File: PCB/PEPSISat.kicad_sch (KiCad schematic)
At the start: 2 parts, among them U1 STM32H747IITx, U2 RP2350A

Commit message: KiCad
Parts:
- added U3: MT48LC16M16A2P, Package_SO:TSOP-II-54_22.2x10.16mm_P0.8mm, symbol Memory_RAM:MT48LC16M16A2P
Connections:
- net at U1.110 (PG2): now also U3.36 (A12)
- net at U1.18 (PF0): now also U3.23 (A0)
- net at U1.19 (PF1): now also U3.24 (A1)
- net at U1.20 (PF2): now also U3.25 (A2)
- net at U1.21 (PF3): now also U3.26 (A3)
- net at U1.22 (PF4): now also U3.29 (A4)
- net at U1.23 (PF5): now also U3.30 (A5)
- net at U1.59 (PF12): now also U3.31 (A6)
- net at U1.60 (PF13): now also U3.32 (A7)
- net at U1.61 (PF14): now also U3.33 (A8)
- net at U1.62 (PF15): now also U3.34 (A9)
- net at U1.63 (PG0): now also U3.22 (A10)
- net at U1.66 (PG1): now also U3.35 (A11)
- new net: U3.1 (VDD), U3.14 (VDD), U3.27 (VDD)
- new net: U3.12 (VSSQ), U3.46 (VSSQ), U3.52 (VSSQ), U3.6 (VSSQ)
- new net: U3.28 (VSS), U3.41 (VSS), U3.54 (VSS)
- new net: U3.3 (VDDQ), U3.43 (VDDQ), U3.49 (VDDQ), U3.9 (VDDQ)
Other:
- moved on the sheet: U1

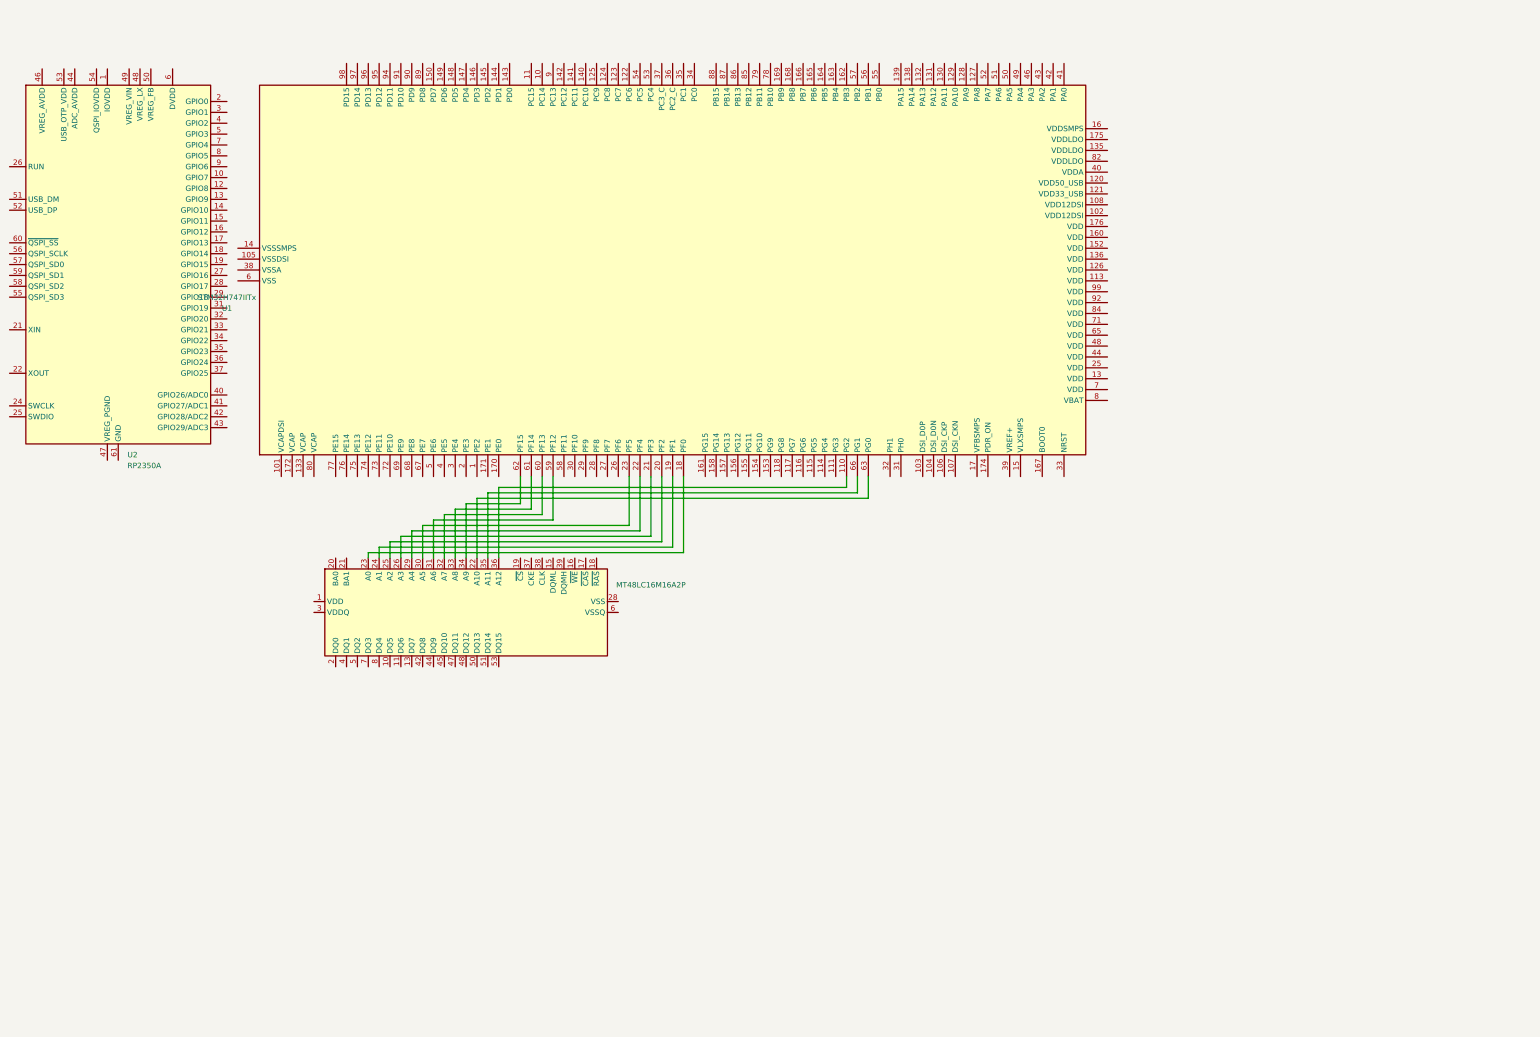
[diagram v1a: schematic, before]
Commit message: KiCad - RAM D&A bus
Added RAM connection for Data and Address bus.
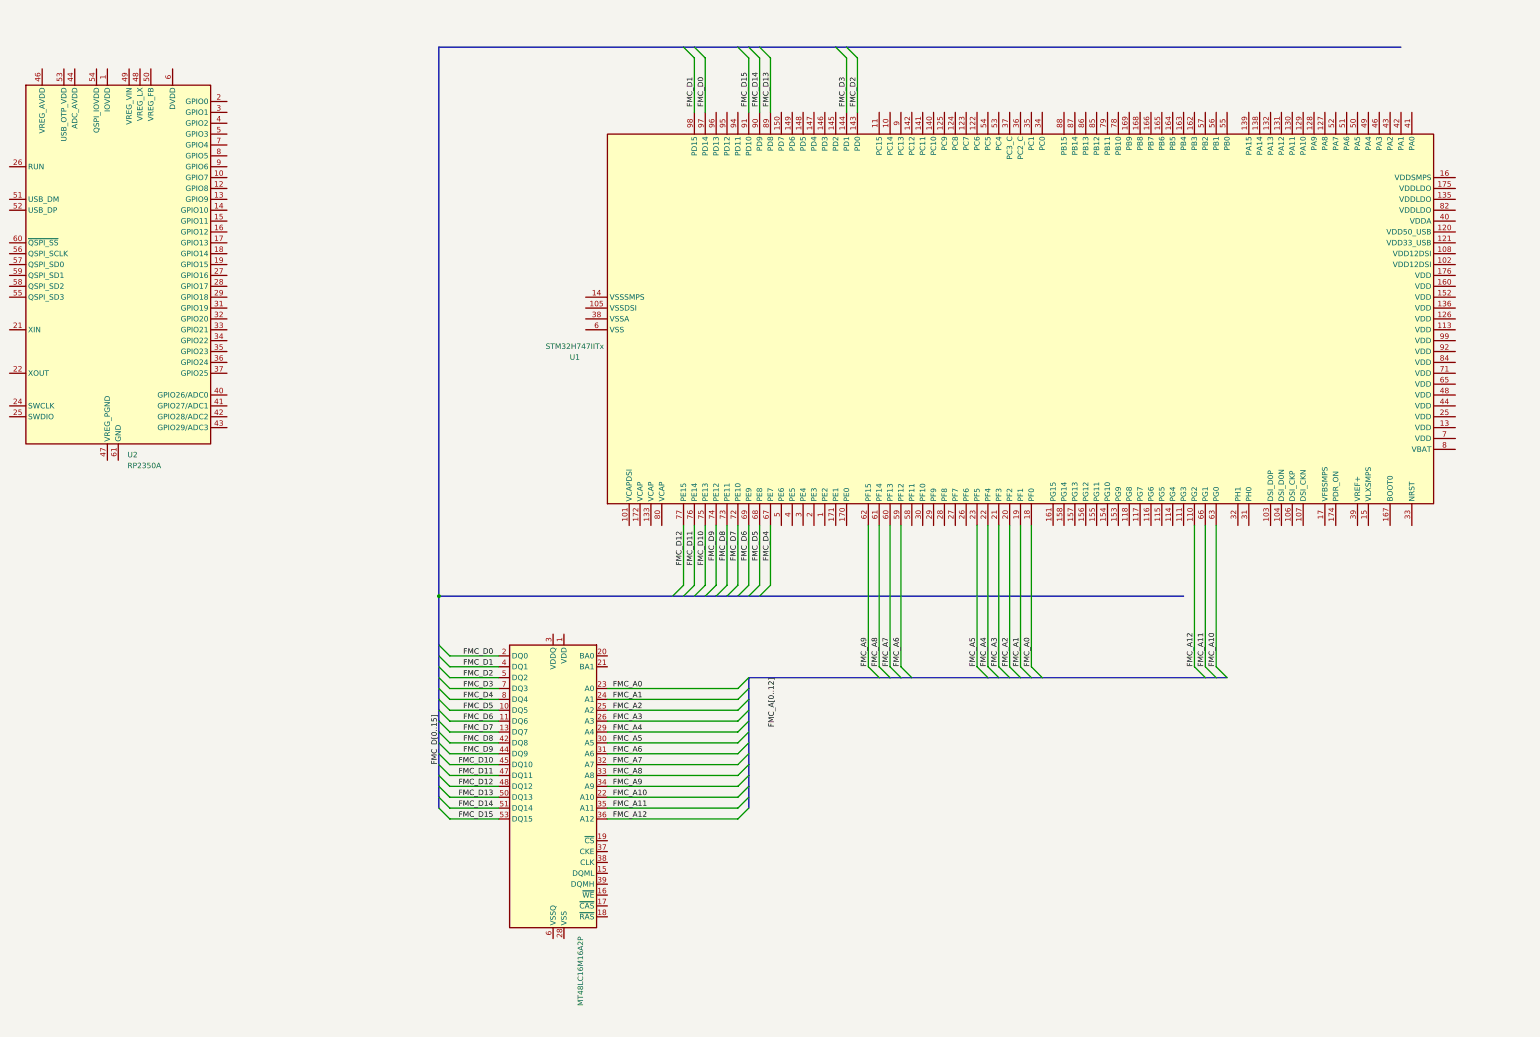
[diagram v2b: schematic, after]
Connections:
- net FMC_D5: now reaches U3.10 (DQ5)
- net FMC_D5: now also U1.68 (PE8)
- net FMC_D6: now reaches U3.11 (DQ6)
- net FMC_D6: now also U1.69 (PE9)
- net FMC_D7: now reaches U3.13 (DQ7)
- net FMC_D7: now also U1.72 (PE10)
- net FMC_D0: now reaches U3.2 (DQ0)
- net FMC_D0: now also U1.97 (PD14)
- net FMC_A10: now reaches U1.63 (PG0), U3.22 (A10)
- net FMC_A0: now reaches U1.18 (PF0), U3.23 (A0)
- net FMC_A1: now reaches U1.19 (PF1), U3.24 (A1)
- net FMC_A2: now reaches U1.20 (PF2), U3.25 (A2)
- net FMC_A3: now reaches U1.21 (PF3), U3.26 (A3)
- net FMC_A4: now reaches U1.22 (PF4), U3.29 (A4)
- net FMC_A5: now reaches U1.23 (PF5), U3.30 (A5)
- net FMC_A6: now reaches U1.59 (PF12), U3.31 (A6)
- net FMC_A7: now reaches U1.60 (PF13), U3.32 (A7)
- net FMC_A8: now reaches U1.61 (PF14), U3.33 (A8)
- net FMC_A9: now reaches U1.62 (PF15), U3.34 (A9)
- net FMC_A11: now reaches U1.66 (PG1), U3.35 (A11)
- net FMC_A12: now reaches U1.110 (PG2), U3.36 (A12)
- net FMC_D1: now reaches U3.4 (DQ1)
- net FMC_D1: now also U1.98 (PD15)
- net FMC_D8: now reaches U3.42 (DQ8)
- net FMC_D8: now also U1.73 (PE11)
- net FMC_D9: now reaches U3.44 (DQ9)
- net FMC_D9: now also U1.74 (PE12)
- net FMC_D10: now reaches U3.45 (DQ10)
- net FMC_D10: now also U1.75 (PE13)
- net FMC_D11: now reaches U3.47 (DQ11)
- net FMC_D11: now also U1.76 (PE14)
- net FMC_D12: now reaches U3.48 (DQ12)
- net FMC_D12: now also U1.77 (PE15)
- net FMC_D2: now reaches U3.5 (DQ2)
- net FMC_D2: now also U1.143 (PD0)
- net FMC_D13: now reaches U3.50 (DQ13)
- net FMC_D13: now also U1.89 (PD8)
- net FMC_D14: now reaches U3.51 (DQ14)
- net FMC_D14: now also U1.90 (PD9)
- net FMC_D15: now reaches U3.53 (DQ15)
- net FMC_D15: now also U1.91 (PD10)
- net FMC_D3: now reaches U3.7 (DQ3)
- net FMC_D3: now also U1.144 (PD1)
- net FMC_D4: now reaches U3.8 (DQ4)
- net FMC_D4: now also U1.67 (PE7)
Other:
- moved on the sheet: U1

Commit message: KiCad
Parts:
- added J1: Conn_02x09_Counter_Clockwise, Connector_PinHeader_2.54mm:PinHeader_2x09_P2.54mm_Horizontal, symbol Connector_Generic:Conn_02x09_Odd_Even
- added U4: BMP280, Package_LGA:Bosch_LGA-8_2x2.5mm_P0.65mm_ClockwisePinNumbering, symbol Sensor_Pressure:BMP280
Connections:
- net at U2.14 (GPIO10): now also U4.4 (SCK)
- net at U2.15 (GPIO11): now also U4.3 (SDI)
- net at U2.16 (GPIO12): now also U4.5 (SDO)
- net at U2.17 (GPIO13): now also U4.2 (CSB)
- net UART.TX: now reaches U2.2 (GPIO0)
- net UART.TX: now also U1.128 (PA9)
- net UART.RX: now reaches U2.3 (GPIO1)
- net UART.RX: now also U1.129 (PA10)
- net UART.RTS_{ST}-CTS_{RP}: now reaches U2.4 (GPIO2)
- net UART.RTS_{ST}-CTS_{RP}: now also U1.131 (PA12)
- net UART.CTS_{ST}-RTS_{RP}: now reaches U2.5 (GPIO3)
- net UART.CTS_{ST}-RTS_{RP}: now also U1.130 (PA11)
- net FMC.DQML: now reaches U3.15 (DQML)
- net FMC.~{WE}: now reaches U3.16 (~{WE})
- net FMC.~{WE}: now also U1.52 (PA7)
- net FMC.~{CAS}: now reaches U3.17 (~{CAS})
- net FMC.~{CAS}: now also U1.161 (PG15)
- net FMC.~{RAS}: now reaches U3.18 (~{RAS})
- net FMC.~{RAS}: now also U1.58 (PF11)
- net FMC.~{CS}: now reaches U3.19 (~{CS})
- net FMC.~{CS}: now also U1.53 (PC4)
- net FMC.BA0: now reaches U3.20 (BA0)
- net FMC.BA0: now also U1.114 (PG4)
- net FMC.BA1: now reaches U3.21 (BA1)
- net FMC.BA1: now also U1.115 (PG5)
- net FMC.CKE: now reaches U3.37 (CKE)
- net FMC.CKE: now also U1.54 (PC5)
- net FMC.CLK: now reaches U3.38 (CLK)
- net FMC.CLK: now also U1.118 (PG8)
- net FMC.DQMH: now reaches U3.39 (DQMH)
- net DCMI.D0: now reaches U1.122 (PC6)
- net DCMI.D0: now also J1.15 (Pin_15)
- net DCMI.D1: now reaches U1.123 (PC7)
- net DCMI.D1: now also J1.16 (Pin_16)
- net DCMI.D2: now reaches U1.124 (PC8)
- net DCMI.D2: now also J1.13 (Pin_13)
- net DCMI.D3: now reaches U1.125 (PC9)
- net DCMI.D3: now also J1.14 (Pin_14)
- net DCMI.XC: now reaches U1.127 (PA8)
- net DCMI.XC: now also J1.7 (Pin_7)
- net DCMI.D5: now reaches U1.146 (PD3)
- net DCMI.D5: now also J1.12 (Pin_12)
- net DCMI.VS: now reaches U1.166 (PB7)
- net DCMI.VS: now also J1.6 (Pin_6)
- net DCMI.SCL: now reaches U1.168 (PB8)
- net DCMI.SCL: now also J1.4 (Pin_4)
- net DCMI.SDA: now reaches U1.169 (PB9)
- net DCMI.SDA: now also J1.3 (Pin_3)
- net DCMI.D4: now reaches U1.3 (PE4)
- net DCMI.D4: now also J1.11 (Pin_11)
- net DCMI.D6: now reaches U1.4 (PE5)
- net DCMI.D6: now also J1.9 (Pin_9)
- net DCMI.D7: now reaches U1.5 (PE6)
- net DCMI.D7: now also J1.10 (Pin_10)
- net DCMI.HS: now reaches U1.50 (PA5)
- net DCMI.HS: now also J1.5 (Pin_5)
- net DCMI.PC: now reaches U1.51 (PA6)
- net DCMI.PC: now also J1.8 (Pin_8)
- new net DCMI.3V: J1.2 (Pin_2)
- new net DCMI.G: J1.1 (Pin_1)
- new net DCMI.PD: J1.17 (Pin_17)
- new net DCMI.RT: J1.18 (Pin_18)
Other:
- moved on the sheet: U1

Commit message: KiCad
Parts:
- added C1, C2: C, symbol Device:C
- added R1, R2: 4.7kR, Resistor_SMD:R_0603_1608Metric, symbol Device:R
- added U5: LSM6DSOXTR, LGA-14L_STM, symbol LSM6DSOXTR:LSM6DSOXTR
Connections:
- net GND: now reaches U1.95 (PD12)
- net GND: now also C1.2, C2.1, R2.2, U5.1 (SDO/SA0), U5.13 (SCL), U5.6 (GND), U5.7 (GND)
- net at U1.96 (PD13): now also R1.2, U5.14 (SDA)
- new net 3V3: C1.1, C2.2, R1.1, R2.1, U5.12 (CS), U5.5 (VDDIO), U5.8 (VDD)

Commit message: KiCad
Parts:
- removed U2: RP2350A, Package_DFN_QFN:QFN-60-1EP_7x7mm_P0.4mm_EP3.4x3.4mm, symbol MCU_RaspberryPi:RP2350A
- removed U4: BMP280, Package_LGA:Bosch_LGA-8_2x2.5mm_P0.65mm_ClockwisePinNumbering, symbol Sensor_Pressure:BMP280
- added U6: HMC5883L, LPCC16_HNW, symbol HMC5883L:HMC5883L
- J1: value Conn_02x09_Counter_Clockwise -> CCloc2x9_DCMI-CAM
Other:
- added sheet RP2350 (RP2350.kicad_sch)
- moved on the sheet: C1, C2, R1, R2, U5
